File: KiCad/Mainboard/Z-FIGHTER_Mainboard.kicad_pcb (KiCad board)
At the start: 2 copper layers, 100 x 150 mm, 52 parts, among them IC1 Z80SIO, J1 DB9_Male_MountingHoles, J2 DB9_Male_MountingHoles, J3 USB_B, J4 Conn_02x13_Odd_Even, J5 Conn_Parallel_User, J6 Conn_PATA, J7 Conn_02x03_Odd_Even, SW1 SW_Push, SW2 SW_DIP_x03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

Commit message: Final routing for rev. 2
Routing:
- net SIO_CTSA: track 26.5 -> 25.3 mm
- net VCC: track 222.7 -> 222.1 mm

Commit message: Final silkscreen rev.2
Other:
- board text added: "CPU Control"
- board text added: "SIO/0 Ch.A"
- board text added: "SIO/0 Ch.B"
- board text added: "X1 ►"
- board text added: "X2 ►"
- board text added: "◄ Ch.A"
- board text added: "◄ Ch.B"

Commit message: Update Z-FIGHTER_Mainboard.kicad_pcb
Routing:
- net GND: track 13.0 -> 8.54 mm
- net D0: track 169.5 -> 173.3 mm
- net A15: track 77.0 -> 80.3 mm
- net D7: track 171.2 -> 174.2 mm
- net D1: track 178.1 -> 180.6 mm
- net #WR: track 216.5 -> 218.8 mm
- net A1: track 162.5 -> 164.6 mm
- net A7: track 36.8 -> 38.9 mm
- net A4: track 36.8 -> 38.7 mm
- net A3: track 36.8 -> 38.7 mm
- net A5: track 36.8 -> 38.7 mm
- net A6: track 36.8 -> 38.6 mm
- net CLOCK2: track 37.7 -> 39.4 mm
- net #INT: track 74.9 -> 73.4 mm
- net D6: track 194.7 -> 195.9 mm
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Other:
- board text added: "Mainboard Rev. 2a"
- board text removed: "Mainboard Rev. 2"

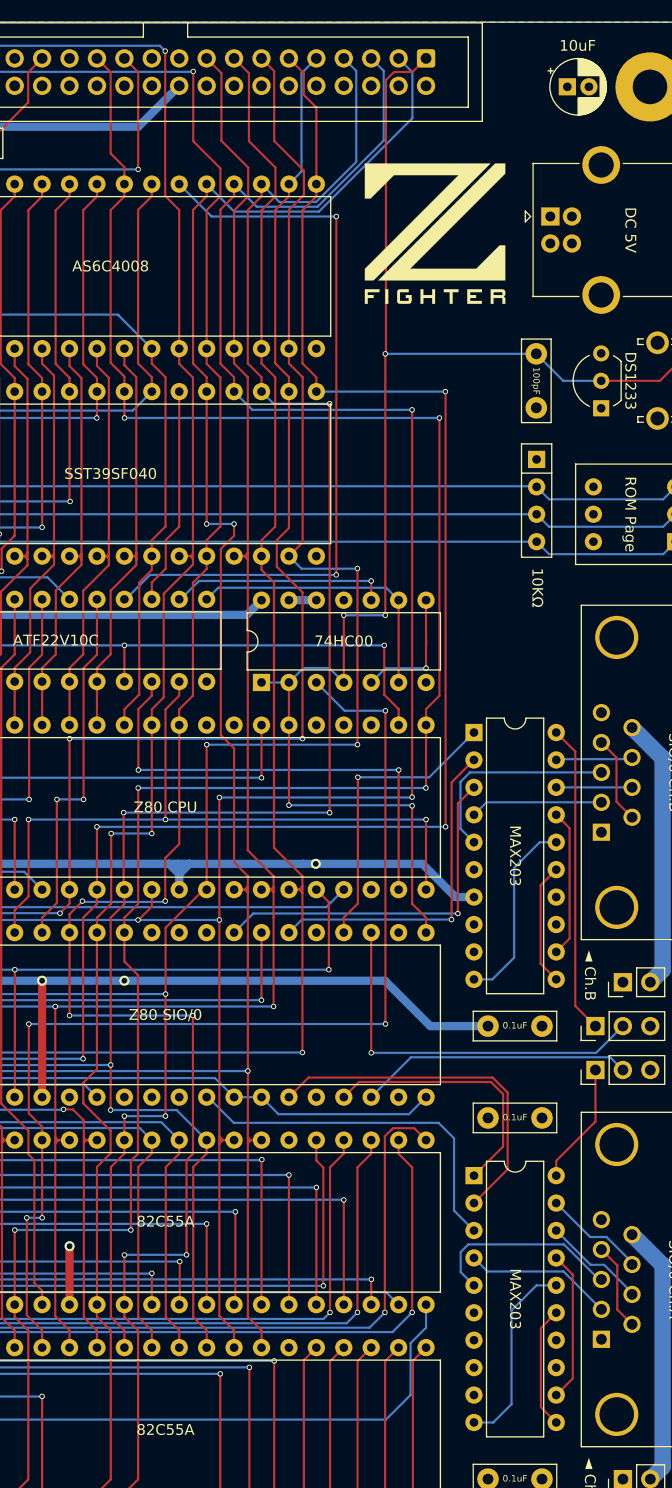
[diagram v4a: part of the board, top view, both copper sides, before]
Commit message: Changed SRAM silkscreen, moved C1, adjusted U6 ground path
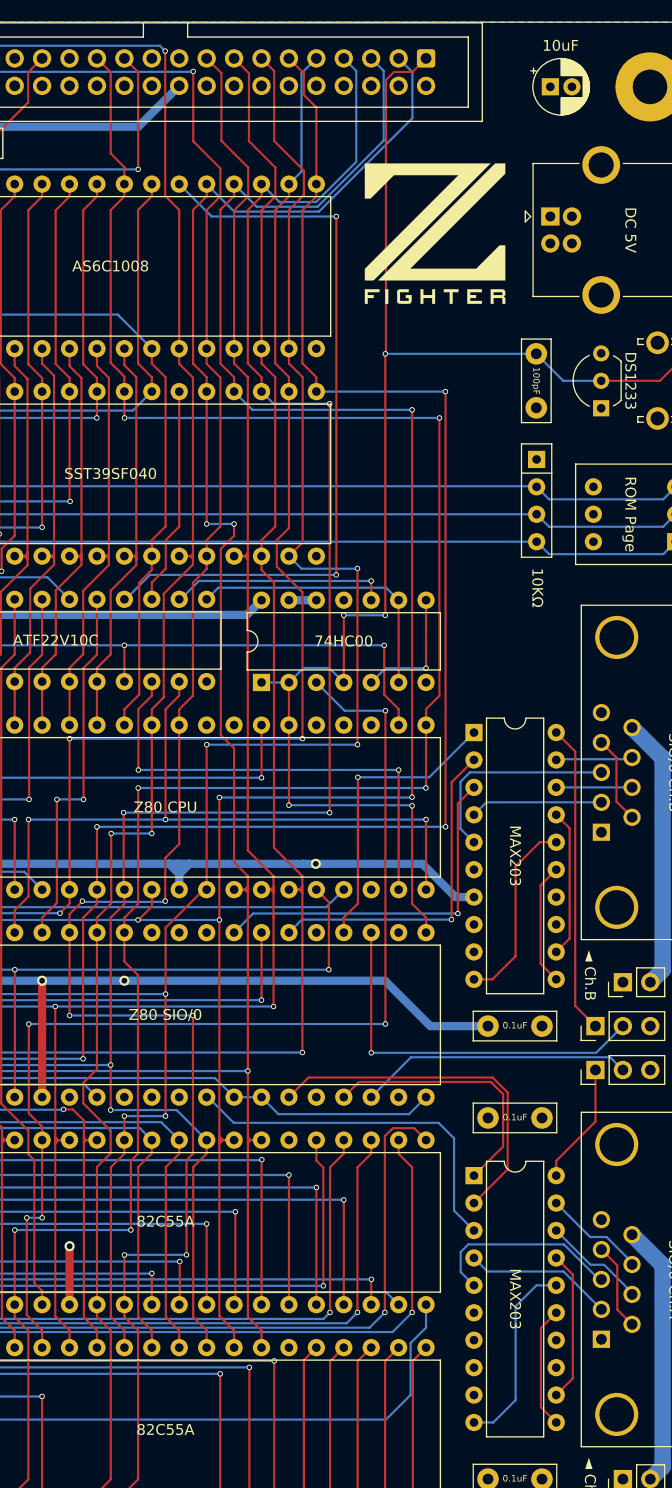
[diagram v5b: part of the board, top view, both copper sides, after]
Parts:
- moved C1 1.58 mm to (122.7, 33.0)

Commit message: Board illustrations
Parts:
- moved C2 30.0 mm to (151.4, 62.7)
- moved J1 30.0 mm to (157.4, 149.0)
- moved J2 30.0 mm to (157.4, 102.0)
- moved RN2 30.0 mm to (151.4, 67.5)
- moved C3 30.0 mm to (84.5, 102.2)
- moved C6 30.0 mm to (88.0, 66.3)
- moved C7 30.0 mm to (88.0, 81.8)
- moved C8 30.0 mm to (88.0, 102.2)
- moved C9 30.0 mm to (84.5, 81.8)
- moved JP1 30.0 mm to (84.5, 120.9)
- moved R1 30.0 mm to (88.0, 105.2)
- moved R2 30.0 mm to (84.5, 105.2)
- moved C1 30.0 mm to (152.7, 33.0)
- moved C10 30.0 mm to (146.9, 161.9)
- moved C11 30.0 mm to (88.0, 115.8)
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
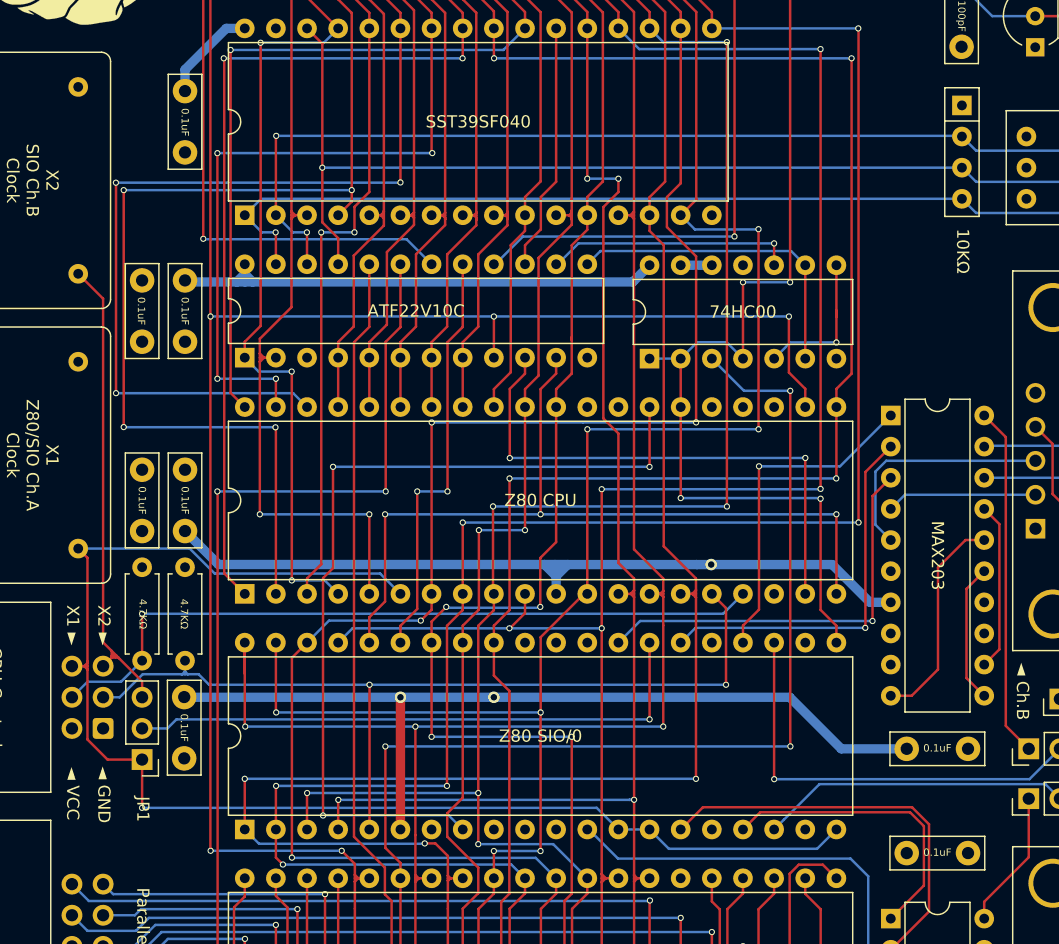
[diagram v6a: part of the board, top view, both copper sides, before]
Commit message: Fixed bypass
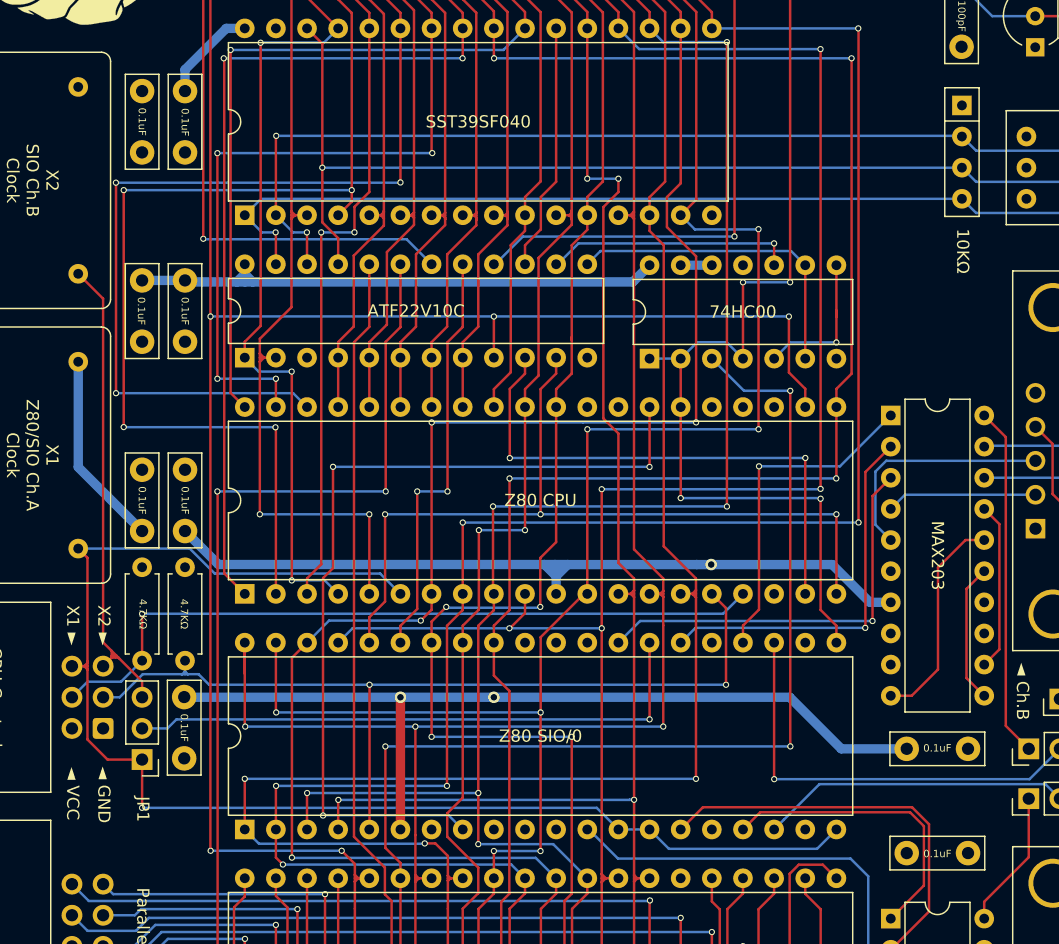
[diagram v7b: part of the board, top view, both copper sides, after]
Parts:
- added C14: 0.1uF, Capacitor_THT:C_Disc_D7.5mm_W2.5mm_P5.00mm, F.Cu at (84.5, 66.3)
- U1: value AS6C4008-55PCN -> AS6C1008-55PCN
- moved C13 5.00 mm to (151.9, 128.5), turned to 180 degrees
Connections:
- C13 pad 1: VCC -> GND
- C13 pad 2: GND -> VCC
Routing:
- net VCC: track 223.2 -> 242.6 mm
